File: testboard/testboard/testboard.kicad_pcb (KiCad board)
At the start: 2 copper layers, 160 x 106 mm, 13 parts, among them IC1 STGIPQ3H60T-HL, J1 Conn_01x02, J10 Conn_01x25, J11 Conn_01x25, J2 Conn_01x04, J3 Conn_01x08, J4 Conn_01x10, J5 Conn_01x02, J6 Conn_01x04, J7 STM32F407G-DISC1-SHIELD, J8 Conn_01x25, J9 Conn_01x25

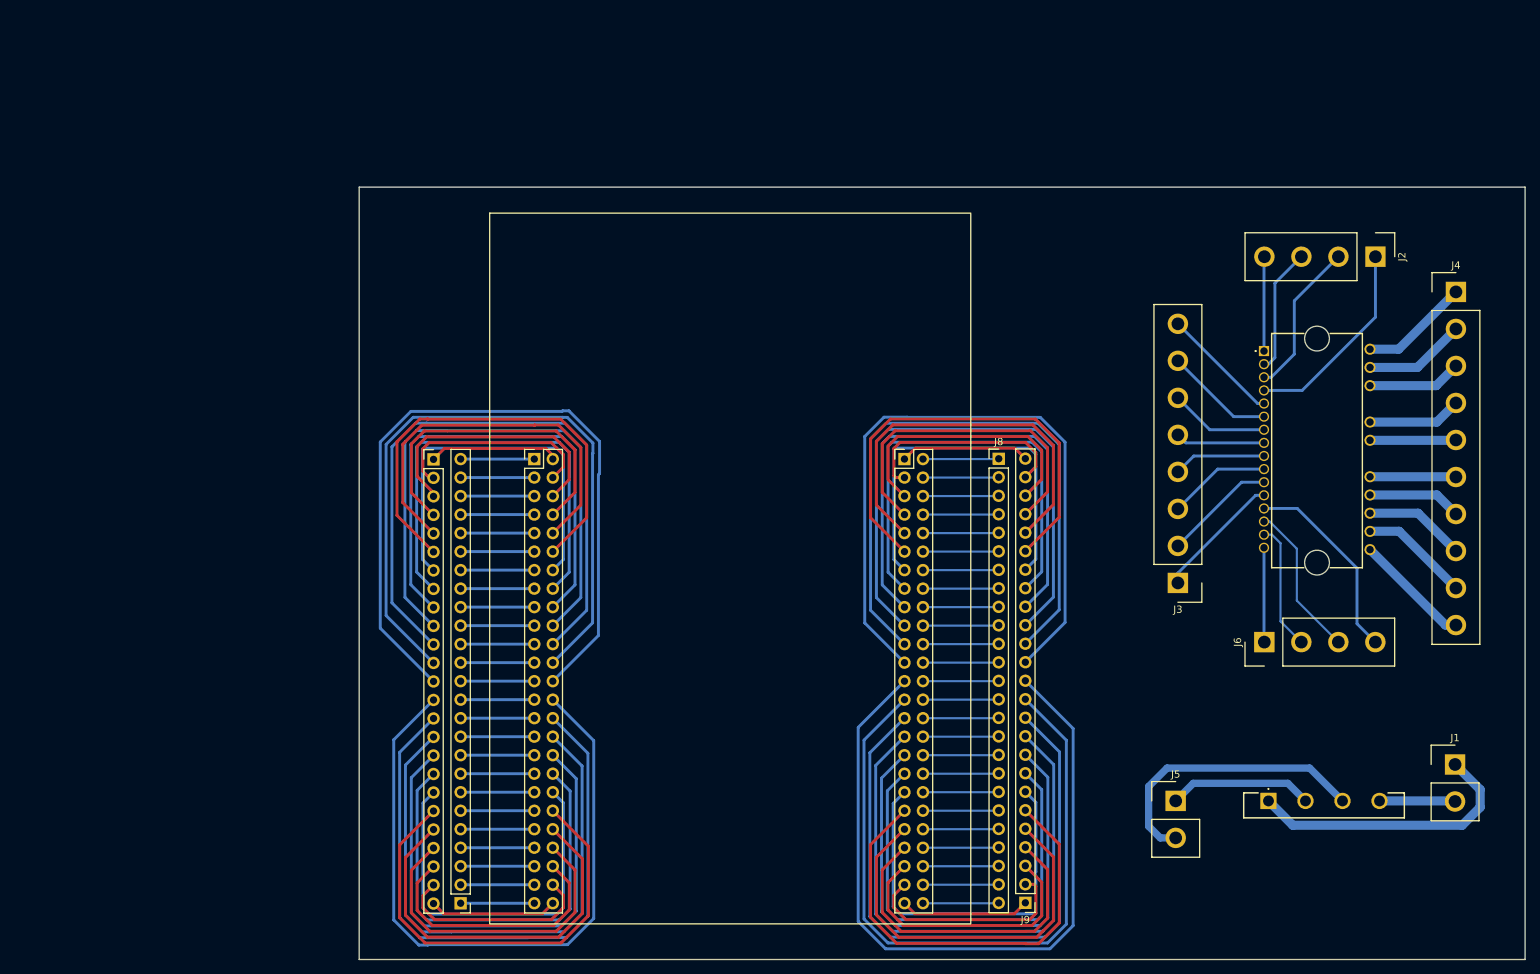
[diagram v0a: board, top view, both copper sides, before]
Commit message: update schematics, BOM, & test board
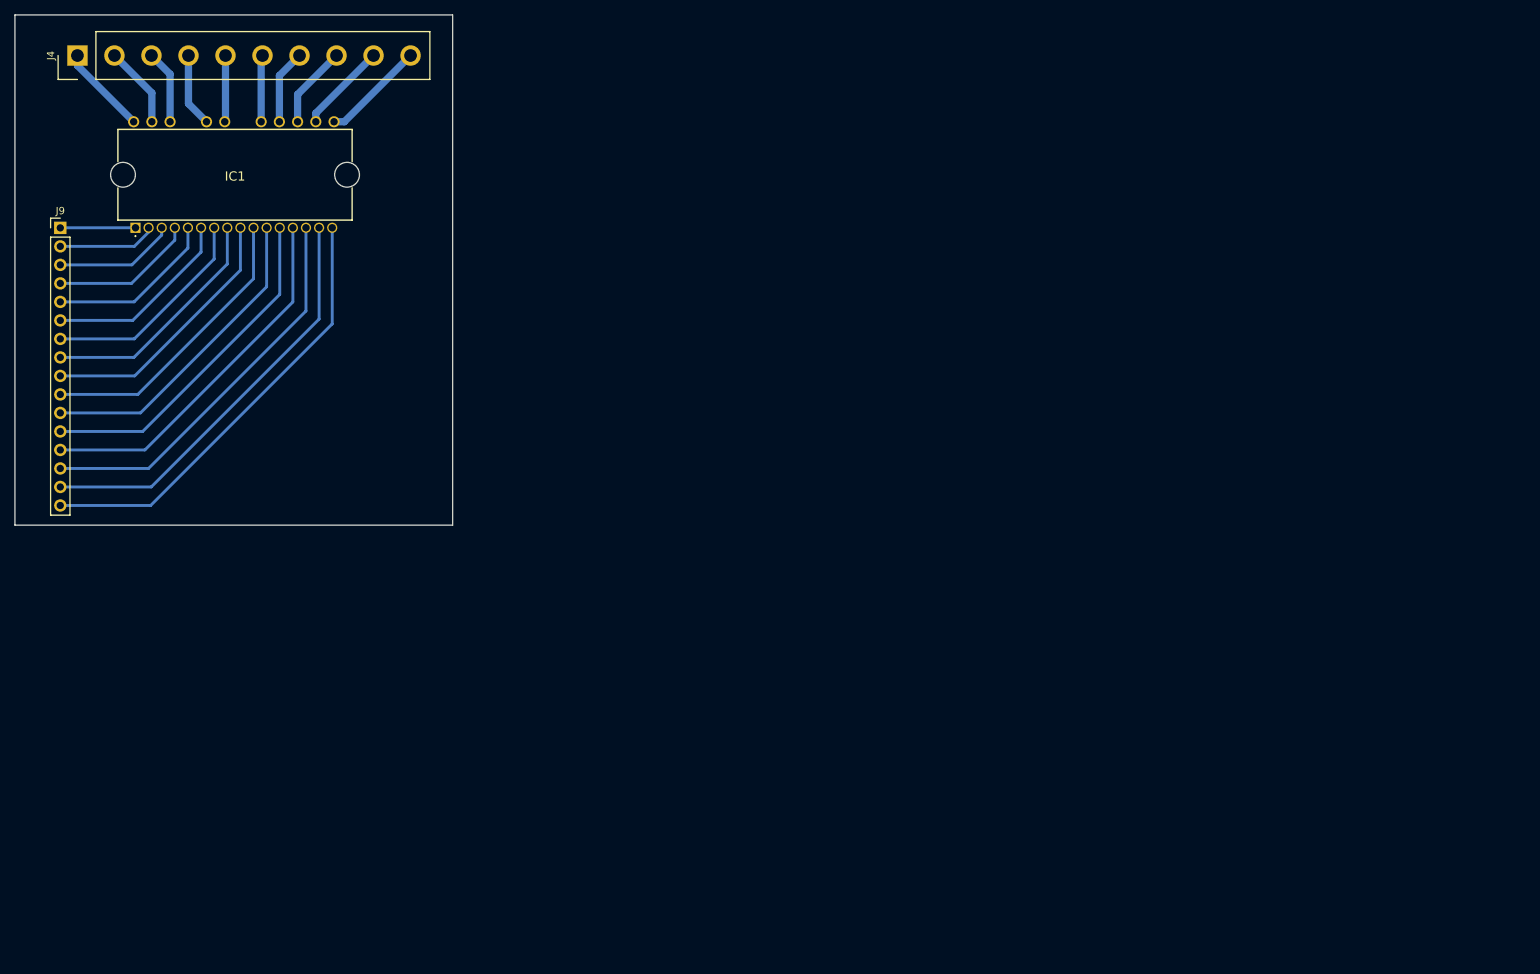
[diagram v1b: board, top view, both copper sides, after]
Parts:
- removed BR1: GBUE2560-M3_P, SamacSys_Parts:GBUE2560M3P
- removed J1, J5: Conn_01x02, Connector_Samtec_HPM_THT:Samtec_HPM-02-01-x-S_Straight_1x02_Pitch5.08mm
- removed J10, J11, J8: Conn_01x25, Connector_PinHeader_2.54mm:PinHeader_1x25_P2.54mm_Vertical
- removed J2, J6: Conn_01x04, Connector_Samtec_HPM_THT:Samtec_HPM-04-01-x-S_Straight_1x04_Pitch5.08mm
- removed J3: Conn_01x08, Connector_Samtec_HPM_THT:Samtec_HPM-08-01-x-S_Straight_1x08_Pitch5.08mm
- removed J7: STM32F407G-DISC1-SHIELD, Custom:STM32F407G-DISC1-SHIELD
- J9: value Conn_01x25 -> Conn_01x16; footprint Connector_PinHeader_2.54mm:PinHeader_1x25_P2.54mm_Vertical -> Connector_PinHeader_2.54mm:PinHeader_1x16_P2.54mm_Vertical
- moved J4 191.9 mm to (37.3, 28.9), turned to 90 degrees
- moved J9 161.6 mm to (35.0, 52.6), turned to 0 degrees
- moved IC1 155.8 mm to (45.3, 52.6), turned to 0 degrees
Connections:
- J9 pad 1: Net-(J9-Pin_1) -> Net-(IC1-GND)
- J9 pad 10: Net-(J7-PD3) -> Net-(IC1-HIN_V_)
- J9 pad 11: Net-(J7-PD5) -> Net-(IC1-LIN_V)
- J9 pad 12: Net-(J7-PD7) -> Net-(IC1-CIN_)
- J9 pad 13: Net-(J7-PB4) -> Net-(IC1-VCC_U)
- J9 pad 14: Net-(J7-PB6) -> Net-(IC1-HIN_U)
- J9 pad 15: Net-(J7-BOOT0) -> Net-(IC1-T/~{SD}/OD)
- J9 pad 16: Net-(J7-PB8) -> Net-(IC1-LIN_U)
- J9 pad 2: Net-(J7-PC6) -> Net-(IC1-T/~{SD}/OD_)
- J9 pad 3: Net-(J7-PC8) -> Net-(IC1-VCC_W_)
- J9 pad 4: Net-(J7-PA8) -> Net-(IC1-HIN_W)
- J9 pad 5: Net-(J7-PA10) -> Net-(IC1-LIN_W)
- J9 pad 6: Net-(J7-PA14) -> Net-(IC1-OP+)
- J9 pad 7: Net-(J7-PC10) -> Net-(IC1-OPOUT)
- J9 pad 8: Net-(J7-PC12) -> Net-(IC1-OP-)
- J9 pad 9: Net-(J7-PD1) -> Net-(IC1-VCC_V)
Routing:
- net Net-(J10-Pin_13): track 105.1 -> 0.00 mm
- net Net-(J7-PB4): track 104.3 -> 0.00 mm
- net Net-(J10-Pin_12): track 96.5 -> 0.00 mm
- net Net-(J7-PD7): track 95.8 -> 0.00 mm
- net Net-(J7-PB6): track 95.8 -> 0.00 mm
- net Net-(J10-Pin_14): track 95.2 -> 0.00 mm
- net Net-(J10-Pin_11): track 88.1 -> 0.00 mm
- net Net-(J7-BOOT0): track 87.3 -> 0.00 mm
- net Net-(J7-PD5): track 87.3 -> 0.00 mm
- net Net-(J10-Pin_15): track 86.6 -> 0.00 mm
- net Net-(J7-PB8): track 78.9 -> 0.00 mm
- net Net-(J7-PD3): track 78.9 -> 0.00 mm
- net Net-(J10-Pin_10): track 78.7 -> 0.00 mm
- net Net-(J10-Pin_16): track 78.2 -> 0.00 mm
- net Net-(J7-PD1): track 70.5 -> 0.00 mm
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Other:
- board size 160 x 106 mm -> 60.1 x 70 mm
